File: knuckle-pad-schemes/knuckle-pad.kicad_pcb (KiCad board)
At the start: 2 copper layers, 127.2 x 115.3 mm, 67 parts, among them SW1 SW_Push, SW10 SW_Push, SW11 SW_Push, SW12 SW_Push, SW13 SW_Push, SW14 SW_Push, SW15 SW_Push, SW16 SW_Push, SW17 SW_Push, SW18 SW_Push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

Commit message: complete rework
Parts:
- removed the D25 at (181.5, 44.7)
- removed the D26 at (181.5, 63.8)
- removed H1, H2, H3, H4, H5, H6: MountingHole, used_footprints:M2_HOLE_PCB
- removed the SW25 at (191.0, 43.4)
- removed the SW26 at (191.0, 62.5)
- SW2, SW3, SW4: footprint MX_Only:MXOnly-1.25U-NoLED -> MX_Only:MXOnly-1U-NoLED
- moved U1 45.0 mm to (197.6, 55.1)
- moved G*** 20.4 mm to (113.7, 118.6)
- moved D5 13.7 mm to (102.9, 122.7)
- moved SW5 13.5 mm to (91.0, 123.7)
- moved SW2 4.71 mm to (91.0, 66.5)
- moved SW3 4.71 mm to (91.0, 85.6)
- moved SW4 4.71 mm to (91.0, 104.6)
- moved SW1 4.06 mm to (91.0, 47.5)
- moved SW15 2.29 mm to (152.9, 45.7)
- moved SW18 2.29 mm to (152.9, 102.9)
- moved SW20 2.29 mm to (172.0, 45.7)
- moved SW23 2.29 mm to (172.0, 102.9)
- moved SW26 2.29 mm to (191.0, 102.9)
- moved SW6 2.29 mm to (114.8, 45.7)
- moved SW9 2.29 mm to (114.8, 102.9)
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- renumbered D27 to D25, D28 to D26, D29 to D27, SW27 to SW25, SW28 to SW26, SW29 to SW27
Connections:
- U1 pad 1: Net-(U1-Pad1) -> unconnected-(U1-Pad1)
- U1 pad 10: col2 -> row3
- U1 pad 11: col1 -> row4
- U1 pad 12: col0 -> unconnected-(U1-Pad12)
- U1 pad 13: col5 -> unconnected-(U1-Pad13)
- U1 pad 14: col4 -> unconnected-(U1-Pad14)
- U1 pad 15: col3 -> col5
- U1 pad 16: Net-(U1-Pad16) -> col4
- U1 pad 17: Net-(U1-Pad17) -> col3
- U1 pad 18: Net-(U1-Pad18) -> col2
- U1 pad 19: Net-(U1-Pad19) -> col1
- U1 pad 2: Net-(U1-Pad2) -> unconnected-(U1-Pad2)
- U1 pad 20: Net-(U1-Pad20) -> col0
- U1 pad 24: Net-(U1-Pad24) -> unconnected-(U1-Pad24)
- U1 pad 5: row0 -> unconnected-(U1-Pad5)
- U1 pad 6: row1 -> unconnected-(U1-Pad6)
- U1 pad 7: row2 -> row0
- U1 pad 8: row3 -> row1
- U1 pad 9: row4 -> row2
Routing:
- net col1: track 113.5 -> 217.8 mm, vias 1 -> 2
- net col2: track 161.5 -> 229.0 mm, vias 0 -> 1
- net col5: track 194.7 -> 130.6 mm, vias 0 -> 1
- net row1: track 139.6 -> 91.4 mm, vias 2 -> 0
- net row4: track 210.7 -> 163.6 mm, vias 3 -> 1
- net col3: track 144.8 -> 190.3 mm, vias 0 -> 1
- net row3: track 173.8 -> 128.8 mm, vias 4 -> 1
- net row2: track 154.6 -> 110.4 mm, vias 4 -> 1
- net col0: track 208.6 -> 252.2 mm, vias 3 -> 1
- net row0: track 123.3 -> 94.4 mm
- net col4: track 157.8 -> 173.6 mm, vias 0 -> 1
- net RST: track 29.8 -> 21.8 mm
- net Net-(D26-Pad2) (its old number): track 5.72 -> 0.00 mm
- net Net-(D25-Pad2) (its old number): track 5.72 -> 0.00 mm
- net Net-(D2-Pad2): track 12.6 -> 15.2 mm
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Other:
- board size 127.2 x 115.3 mm -> 128 x 115.3 mm
- net class Default removed

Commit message: prelim version before trying to fit mcu cover and sw plate
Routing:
- net row1: track 91.4 -> 95.1 mm
- net row3: track 128.8 -> 126.8 mm
- net row4: track 163.6 -> 163.0 mm

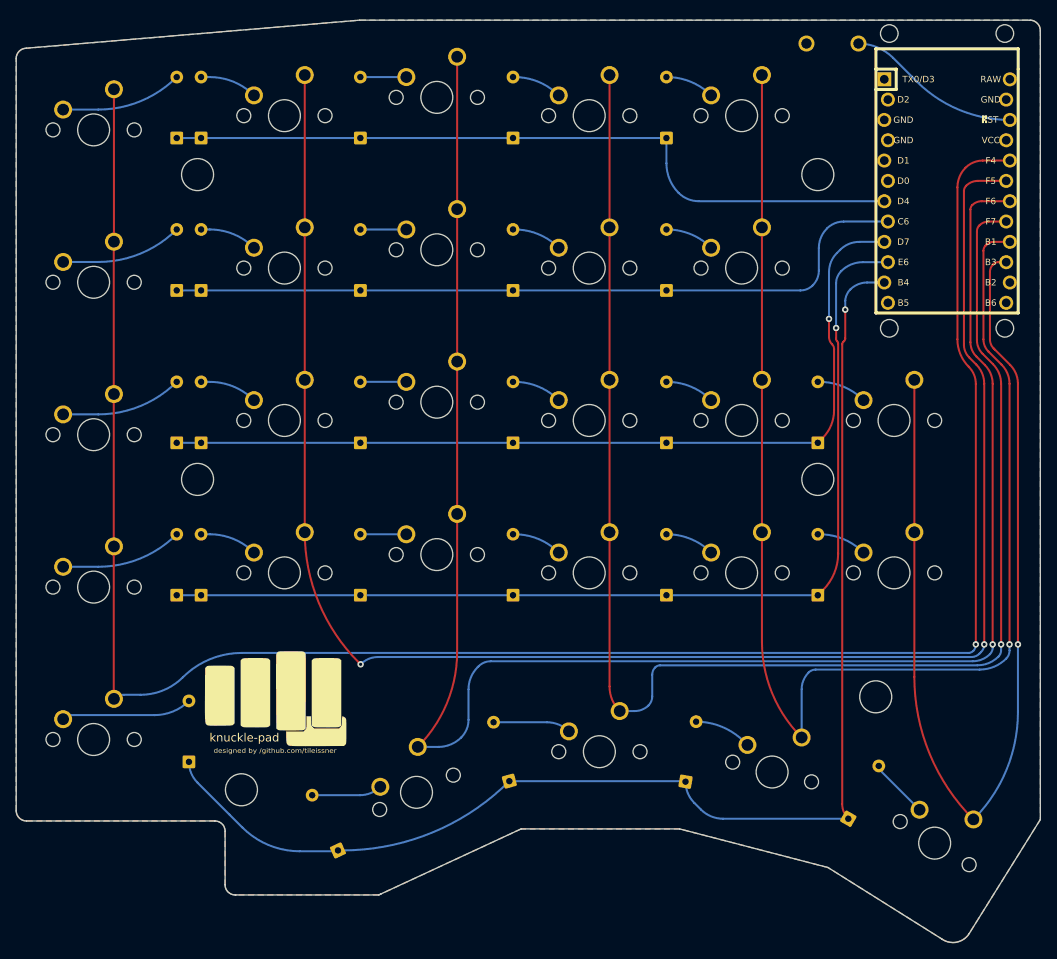
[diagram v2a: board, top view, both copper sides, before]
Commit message: moved mcu and switched back to traymount
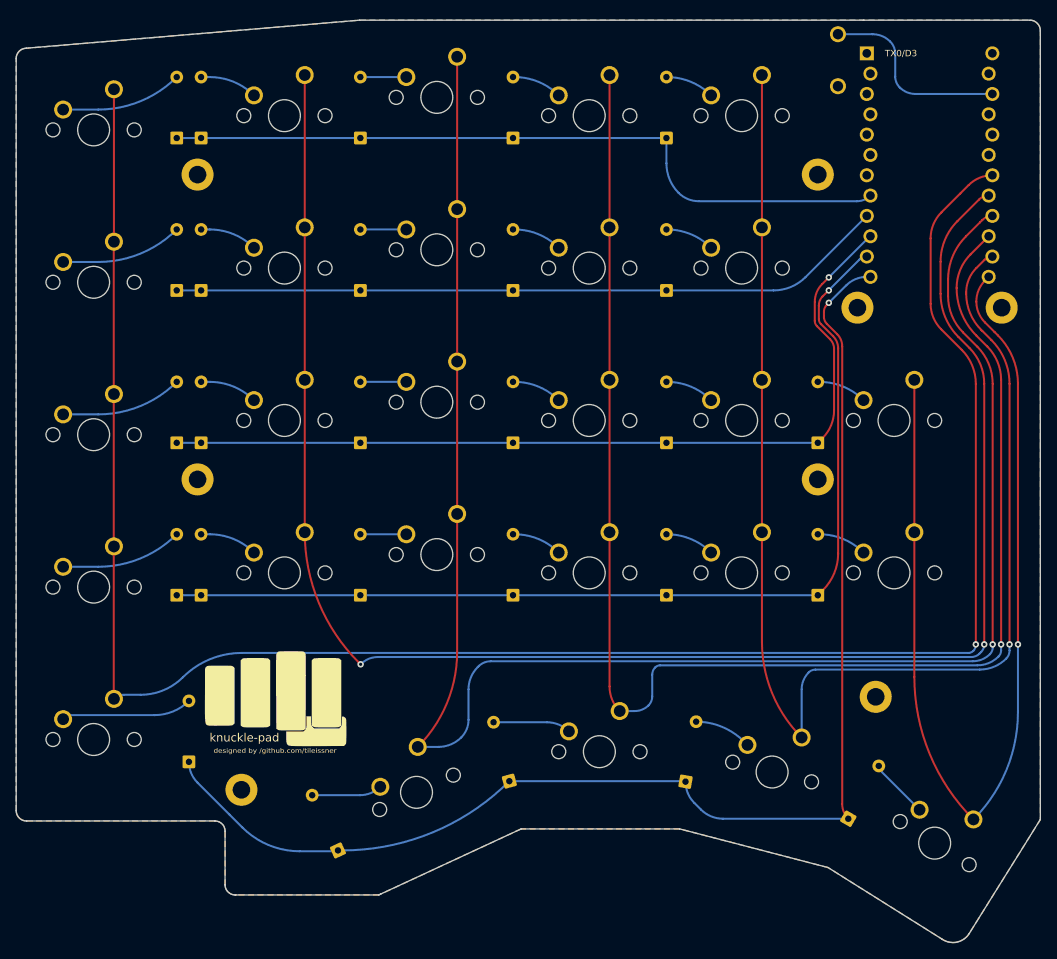
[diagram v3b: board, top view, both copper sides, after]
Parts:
- added H1: Hole, used_footprints:M2_HOLE_PCB, F.Cu at (103.9, 53.1)
- added H2: Hole, used_footprints:M2_HOLE_PCB, F.Cu at (103.9, 91.2)
- added H3: Hole, used_footprints:M2_HOLE_PCB, F.Cu at (109.4, 130.0)
- added H4: Hole, used_footprints:M2_HOLE_PCB, F.Cu at (181.5, 53.1)
- added H5: Hole, used_footprints:M2_HOLE_PCB, F.Cu at (181.5, 91.2)
- added H6: Hole, used_footprints:M2_HOLE_PCB, F.Cu at (188.7, 118.4)
- added H7: Hole, used_footprints:M2_HOLE_PCB, F.Cu at (186.4, 69.7)
- added H8: Hole, used_footprints:M2_HOLE_PCB, F.Cu at (204.5, 69.7)
- moved U1 3.91 mm to (195.5, 51.9)
- moved RST1 2.19 mm to (184.0, 38.8), turned to 90 degrees
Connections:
- U1 pad 10: row3 -> row2
- U1 pad 11: row4 -> row3
- U1 pad 12: unconnected-(U1-Pad12) -> row4
- U1 pad 13: unconnected-(U1-Pad13) -> col5
- U1 pad 14: unconnected-(U1-Pad14) -> col4
- U1 pad 15: col5 -> col3
- U1 pad 16: col4 -> col2
- U1 pad 17: col3 -> col1
- U1 pad 18: col2 -> col0
- U1 pad 19: col1 -> unconnected-(U1-Pad19)
- U1 pad 20: col0 -> unconnected-(U1-Pad20)
- U1 pad 7: row0 -> unconnected-(U1-Pad7)
- U1 pad 8: row1 -> row0
- U1 pad 9: row2 -> row1
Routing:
- net row1: track 95.1 -> 89.8 mm
- net col1: track 217.8 -> 214.7 mm
- net col2: track 229.0 -> 225.8 mm
- net col3: track 190.3 -> 187.4 mm
- net RST: track 21.8 -> 24.6 mm
- net col4: track 173.6 -> 170.9 mm
- net col5: track 130.6 -> 128.0 mm
- net col0: track 252.2 -> 250.3 mm
- net row0: track 94.4 -> 92.9 mm
- net row2: track 110.4 -> 109.4 mm
- net row3: track 126.8 -> 125.8 mm
- net row4: track 163.0 -> 164.0 mm
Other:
- outline, holes or cut-outs redrawn
